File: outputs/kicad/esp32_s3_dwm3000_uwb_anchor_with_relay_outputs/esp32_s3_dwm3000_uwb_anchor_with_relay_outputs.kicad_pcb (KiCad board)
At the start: 2 copper layers, 120 x 80 mm, 3 parts, among them J2 SMA antenna connector, U1 ESP32-S3 module, U2 External connector

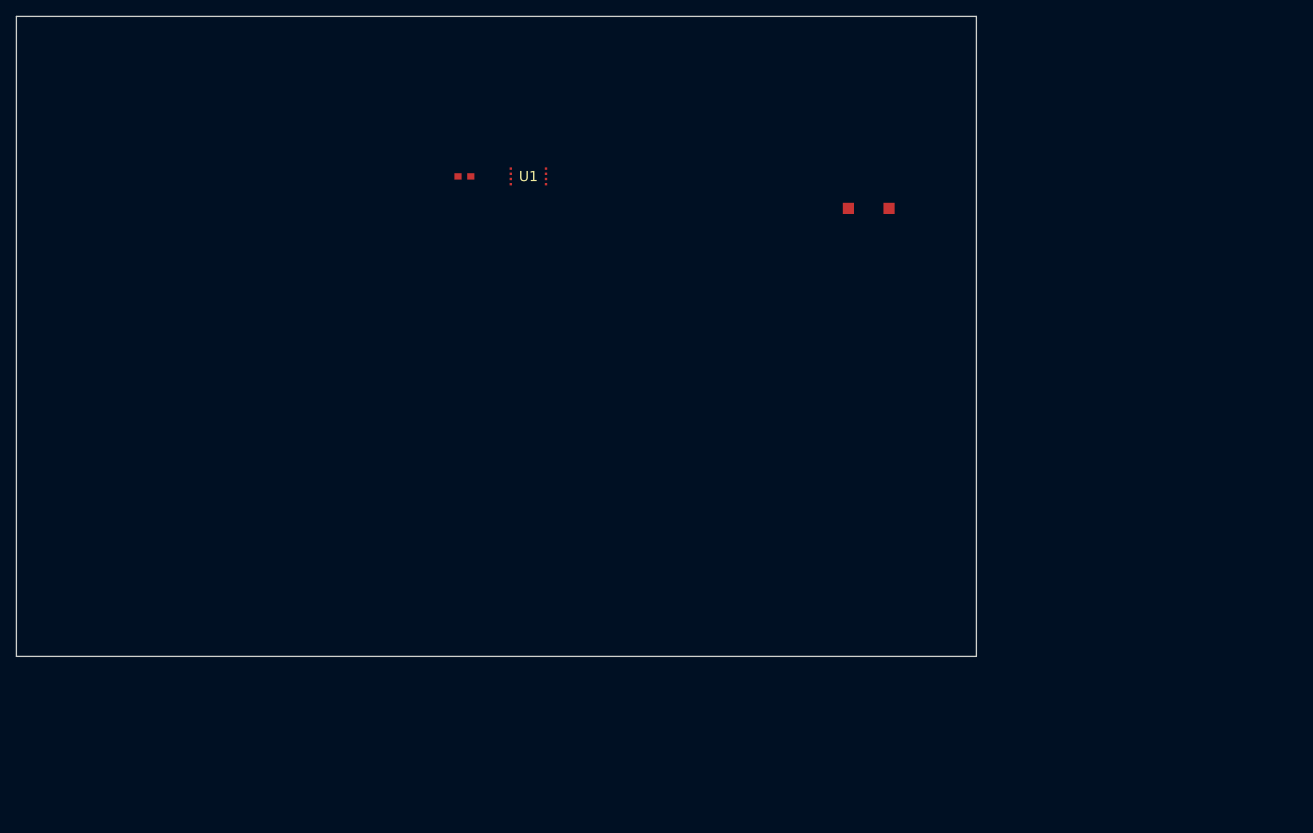
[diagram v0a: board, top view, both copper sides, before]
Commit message: Fix PCBA manufacturing export: Unicode error + asset file sync
- Fixed UnicodeEncodeError in pcba_manufacturing_export_service.py (checkmark → [OK])
- Generated real manufacturing package: 27 Gerber files + BOM + documentation
- Synchronized pcba_manufacturing_package.json to assets/generated/ for Flutter access
- Verified both K1 and K2 relays present in schematic, PCB, and manufacturing BOM
- Updated Brainmypcb documentation with manufacturing export status
- Board size confirmed: 160×100 mm, 4-layer, 59 components, DRC clean
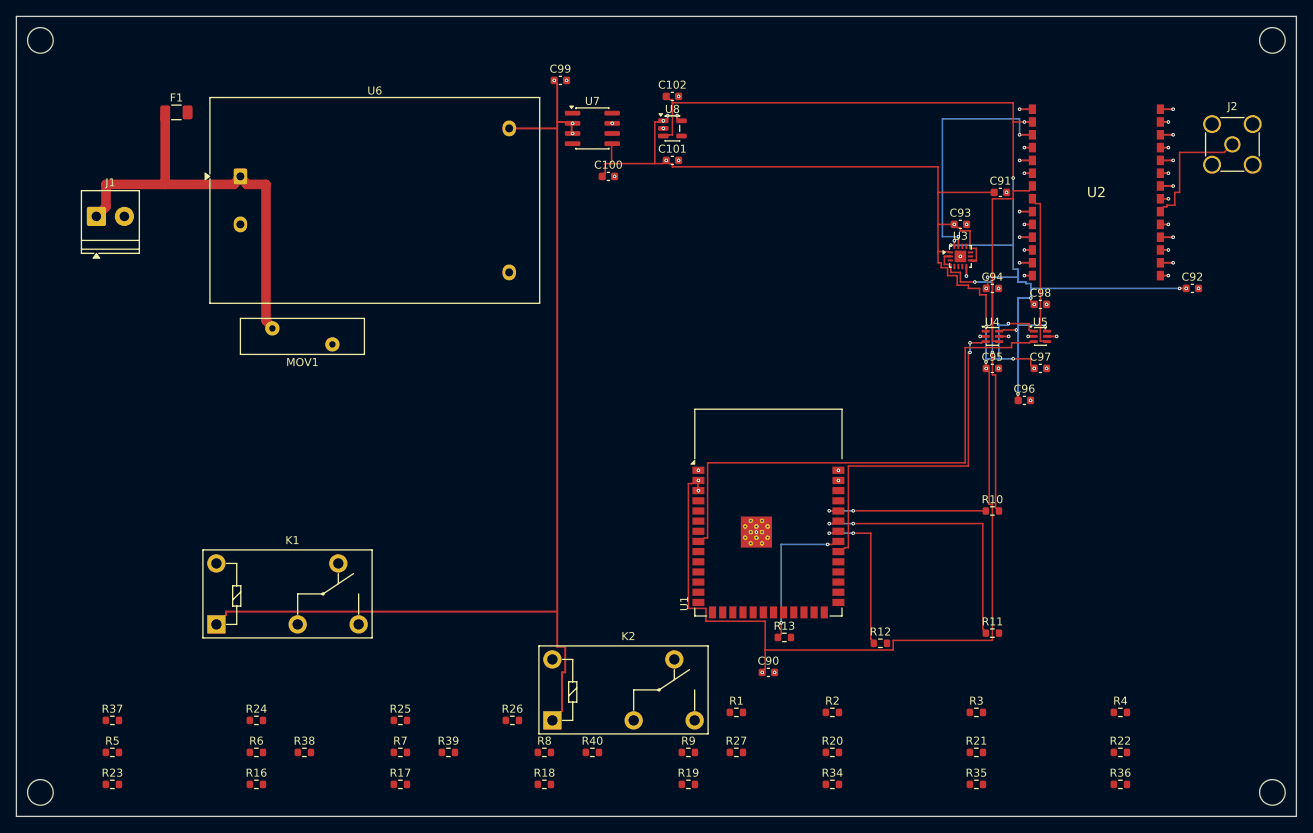
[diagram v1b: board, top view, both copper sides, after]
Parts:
- added C100: 100nF, C_0603_1608Metric, F.Cu at (74.0, 20.0)
- added C101: 100nF, C_0603_1608Metric, F.Cu at (82.0, 18.0)
- added C102: 100nF, C_0603_1608Metric, F.Cu at (82.0, 10.0)
- added C90: 100nF, C_0603_1608Metric, F.Cu at (94.0, 82.0)
- added C91: 100nF, C_0603_1608Metric, F.Cu at (123.0, 22.0)
- added C92: 100nF, C_0603_1608Metric, F.Cu at (147.0, 34.0)
- added C93: 100nF, C_0603_1608Metric, F.Cu at (118.0, 26.0)
- added C94: 100nF, C_0603_1608Metric, F.Cu at (122.0, 34.0)
- added C95: 100nF, C_0603_1608Metric, F.Cu at (122.0, 44.0)
- added C96: 100nF, C_0603_1608Metric, F.Cu at (126.0, 48.0)
- added C97: 100nF, C_0603_1608Metric, F.Cu at (128.0, 44.0)
- added C98: 100nF, C_0603_1608Metric, F.Cu at (128.0, 36.0)
- added C99: 100nF, C_0603_1608Metric, F.Cu at (68.0, 8.00)
- added F1: 500mA fuse, Fuse_1206_3216Metric, F.Cu at (20.0, 12.0)
- added J1: AC Şebeke Girişi, TerminalBlock_Phoenix_PT-1,5-2-3.5-H_1x02_P3.50mm_Horizontal, F.Cu at (10.0, 25.0)
- added K1: 5V relay, Relay_SPDT_Omron-G5Q-1, F.Cu at (25.0, 76.0)
- added K2: 5V relay, Relay_SPDT_Omron-G5Q-1, F.Cu at (67.0, 88.0)
- added MOV1: AC varistor, RV_Disc_D15.5mm_W4.5mm_P7.5mm, F.Cu at (32.0, 39.0)
- added R1: 100R, R_0603_1608Metric, F.Cu at (90.0, 87.0)
- added R10: 100R, R_0603_1608Metric, F.Cu at (122.0, 61.8)
- added R11: 100R, R_0603_1608Metric, F.Cu at (122.0, 77.1)
- added R12: 100R, R_0603_1608Metric, F.Cu at (108.0, 78.4)
- added R13: 100R, R_0603_1608Metric, F.Cu at (96.0, 77.6)
- added R16: 100R, R_0603_1608Metric, F.Cu at (30.0, 96.0)
- added R17: 100R, R_0603_1608Metric, F.Cu at (48.0, 96.0)
- added R18: 100R, R_0603_1608Metric, F.Cu at (66.0, 96.0)
- added R19: 100R, R_0603_1608Metric, F.Cu at (84.0, 96.0)
- added R2: 100R, R_0603_1608Metric, F.Cu at (102.0, 87.0)
- added R20: 10K, R_0603_1608Metric, F.Cu at (102.0, 92.0)
- added R21: 33R, R_0603_1608Metric, F.Cu at (120.0, 92.0)
- added R22: 100R, R_0603_1608Metric, F.Cu at (138.0, 92.0)
- added R23: 100R, R_0603_1608Metric, F.Cu at (12.0, 96.0)
- added R24: 100R, R_0603_1608Metric, F.Cu at (30.0, 88.0)
- added R25: 100R, R_0603_1608Metric, F.Cu at (48.0, 88.0)
- added R26: 100R, R_0603_1608Metric, F.Cu at (62.0, 88.0)
- added R27: 100R, R_0603_1608Metric, F.Cu at (90.0, 92.0)
- added R3: 100R, R_0603_1608Metric, F.Cu at (120.0, 87.0)
- added R34: 100R, R_0603_1608Metric, F.Cu at (102.0, 96.0)
- added R35: 100R, R_0603_1608Metric, F.Cu at (120.0, 96.0)
- added R36: 100R, R_0603_1608Metric, F.Cu at (138.0, 96.0)
- added R37: 100R, R_0603_1608Metric, F.Cu at (12.0, 88.0)
- added R38: 100R, R_0603_1608Metric, F.Cu at (36.0, 92.0)
- added R39: 100R, R_0603_1608Metric, F.Cu at (54.0, 92.0)
- added R4: 100R, R_0603_1608Metric, F.Cu at (138.0, 87.0)
- added R40: 100R, R_0603_1608Metric, F.Cu at (72.0, 92.0)
- added R5: 100R, R_0603_1608Metric, F.Cu at (12.0, 92.0)
- added R6: 100R, R_0603_1608Metric, F.Cu at (30.0, 92.0)
- added R7: 100R, R_0603_1608Metric, F.Cu at (48.0, 92.0)
- added R8: 100R, R_0603_1608Metric, F.Cu at (66.0, 92.0)
- added R9: 100R, R_0603_1608Metric, F.Cu at (84.0, 92.0)
- added U3: 4-bit level shifter, WQFN-14-1EP_2.5x2.5mm_P0.5mm_EP1.45x1.45mm, F.Cu at (118.0, 30.0)
- added U4: Single-bit level shifter, SOT-363_SC-70-6, F.Cu at (122.0, 40.0)
- added U5: Single-bit level shifter, SOT-363_SC-70-6, F.Cu at (128.0, 40.0)
- added U6: 5V isolated AC/DC, Converter_ACDC_Hi-Link_HLK-5Mxx, F.Cu at (28.0, 20.0)
- added U7: 3.3V buck, SOIC-8_3.9x4.9mm_P1.27mm, F.Cu at (72.0, 14.0)
- added U8: 1.8V low-noise LDO, SOT-23-5, F.Cu at (82.0, 14.0)
- J2: value SMA antenna connector -> SMA Anten Konektörü; footprint (none) -> SMA_Amphenol_901-144_Vertical
- U1: footprint (none) -> ESP32-S3-WROOM-1
- U2: value External connector -> UWB module; footprint (none) -> OmniCircuit:DWM3000
- moved U2 79.0 mm to (135.0, 22.0)
- moved U1 51.6 mm to (94.0, 62.0)
- moved J2 48.7 mm to (152.0, 16.0)
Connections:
- J2 pad 2: (no net) -> GND
- U1 pad 1: (no net) -> GND
- U1 pad 2: (no net) -> +3V3
- U1 pad 3: (no net) -> +3V3
- U1 pad 4: (no net) -> NC_U1_4_98
- U1 pad 5: (no net) -> NC_U1_5_99
- U1 pad 6: (no net) -> NC_U1_6_100
- U1 pad 7: (no net) -> NC_U1_7_101
- U1 pad 8: (no net) -> DWM_EXT_TX_3V3
- U2 pad 1: (no net) -> GND
- U2 pad 2: (no net) -> +1V8
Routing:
- net +3V3: track 0.00 -> 223.7 mm, vias 0 -> 14
- net +1V8: track 0.00 -> 134.9 mm, vias 0 -> 13
- net +5V_ISO: track 0.00 -> 134.8 mm, vias 0 -> 3
- net DWM_EXT_TX_3V3: track 0.00 -> 66.4 mm
- net AC_L_PROTECTED: track 0.00 -> 52.7 mm
- net DWM_IRQ_3V3: track 0.00 -> 44.2 mm, vias 0 -> 2
- net SPI_CS_3V3: track 0.00 -> 39.8 mm, vias 0 -> 2
- net GND: track 0.00 -> 34.6 mm, vias 0 -> 48
- net SPI_MOSI_3V3_MCU: track 0.00 -> 34.2 mm, vias 0 -> 2
- net SPI_CS_1V8: track 0.00 -> 31.2 mm, vias 0 -> 2
- net DWM_IRQ_1V8: track 0.00 -> 25.0 mm
- net SPI_CS_3V3_MCU: track 0.00 -> 20.7 mm, vias 0 -> 2
- net SPI_CLK_3V3_MCU: track 0.00 -> 20.3 mm, vias 0 -> 2
- net DWM_EXT_TX_1V8: track 0.00 -> 19.4 mm
- net SPI_MISO_3V3_MCU: track 0.00 -> 19.0 mm, vias 0 -> 2
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- added copper zone on In2.Cu, net +1V8
- added copper zone on In2.Cu, net +3V3
- added copper zone on In2.Cu, net +5V_ISO
- added copper zone on In1.Cu, net GND
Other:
- board size 120 x 80 mm -> 160 x 100 mm
- copper layers 2 -> 4
